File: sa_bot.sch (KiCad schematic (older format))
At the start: 61 parts, among them CON1 MicroSD_Card, P1 USB_OTG, P11 MOTOR_A, P12 MOTOR_B, P13 SONAR_4, P14 SONAR_2, P15 SONAR_3, P17 DBG_CONN, P18 CONN_01X04, P2 BatteryHolder, P3 IR4_JMP, P4 IR2_JMP, P5 IR3_JMP, P6 ExPower, P7 IR_4, P8 IR_2, P9 IR_3, Q1 Q_PMOS_DSG, SW1 SWITCH_INV, SW2 SW_PUSH, SW3 SW_PUSH, SW4 SW_PUSH, U1 74AHC1G125, U2 SAMD21G18, U3 AP2112K-3.3V, U4 NCP1402, U5 DRV8835, Y1 Crystal_Small

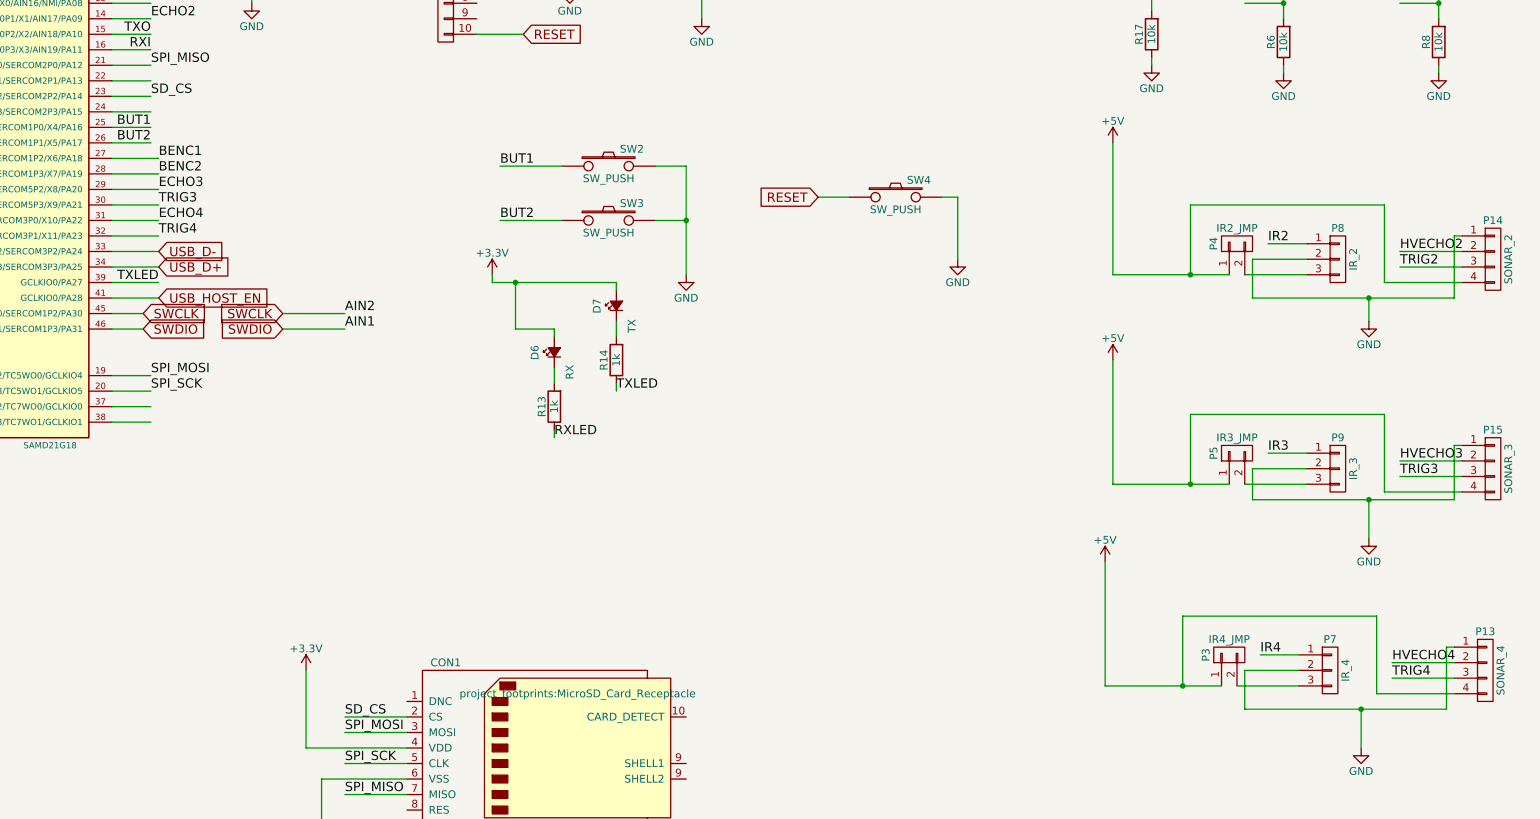
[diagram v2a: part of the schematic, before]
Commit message: Fixed encoder Interrupt
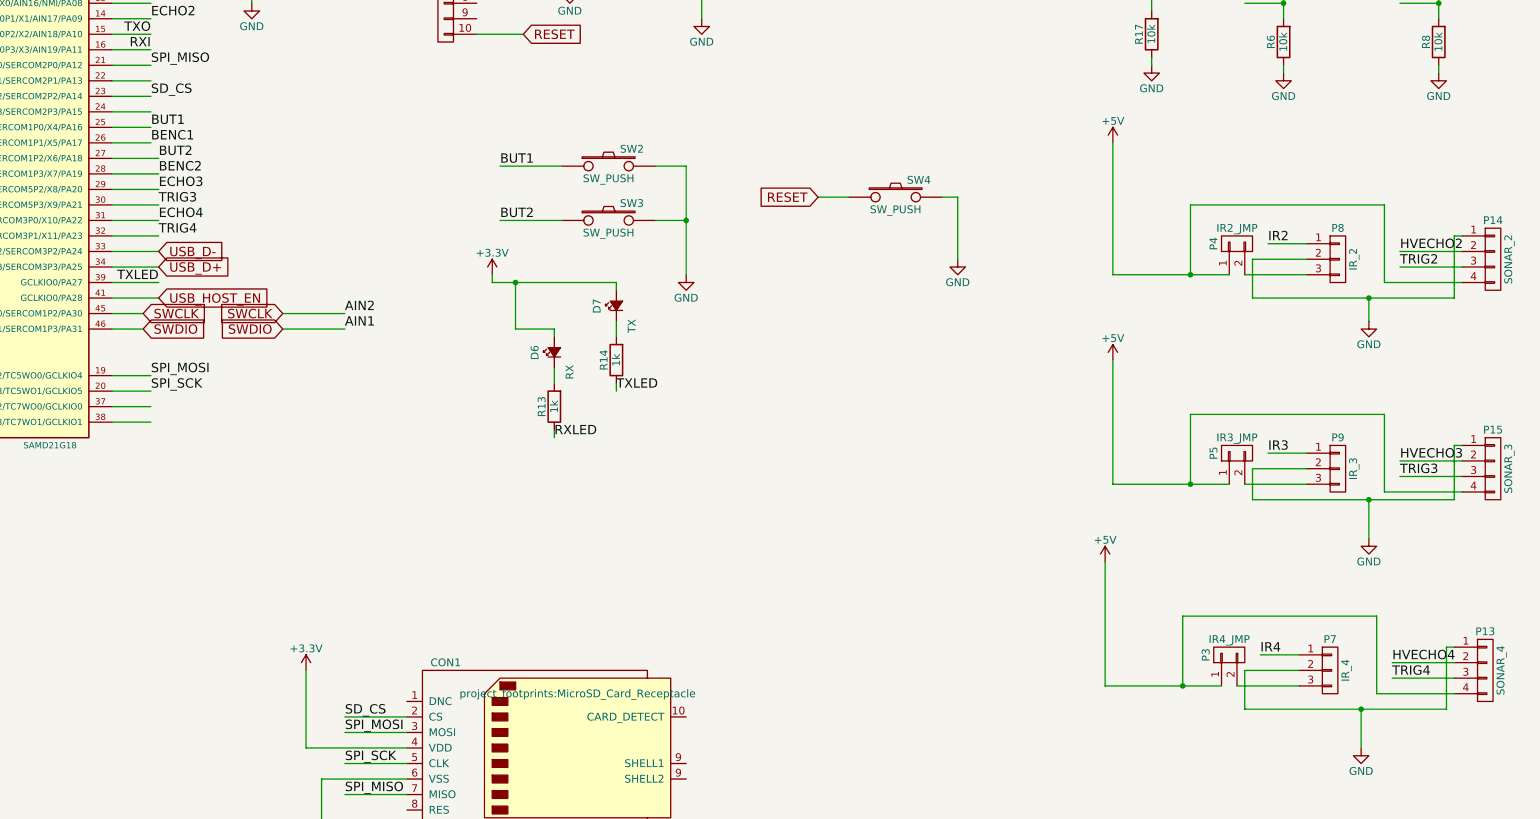
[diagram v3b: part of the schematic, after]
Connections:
- net BENC1: now also U2.26 (GCLKIO3/TC2WO1/SERCOM3P1/SERCOM1P1/X5/PA17); no longer U2.27 (ACCMP0/TC3WO0/SERCOM3P2/SERCOM1P2/X6/PA18)
- net BUT2: now also U2.27 (ACCMP0/TC3WO0/SERCOM3P2/SERCOM1P2/X6/PA18); no longer U2.26 (GCLKIO3/TC2WO1/SERCOM3P1/SERCOM1P1/X5/PA17)

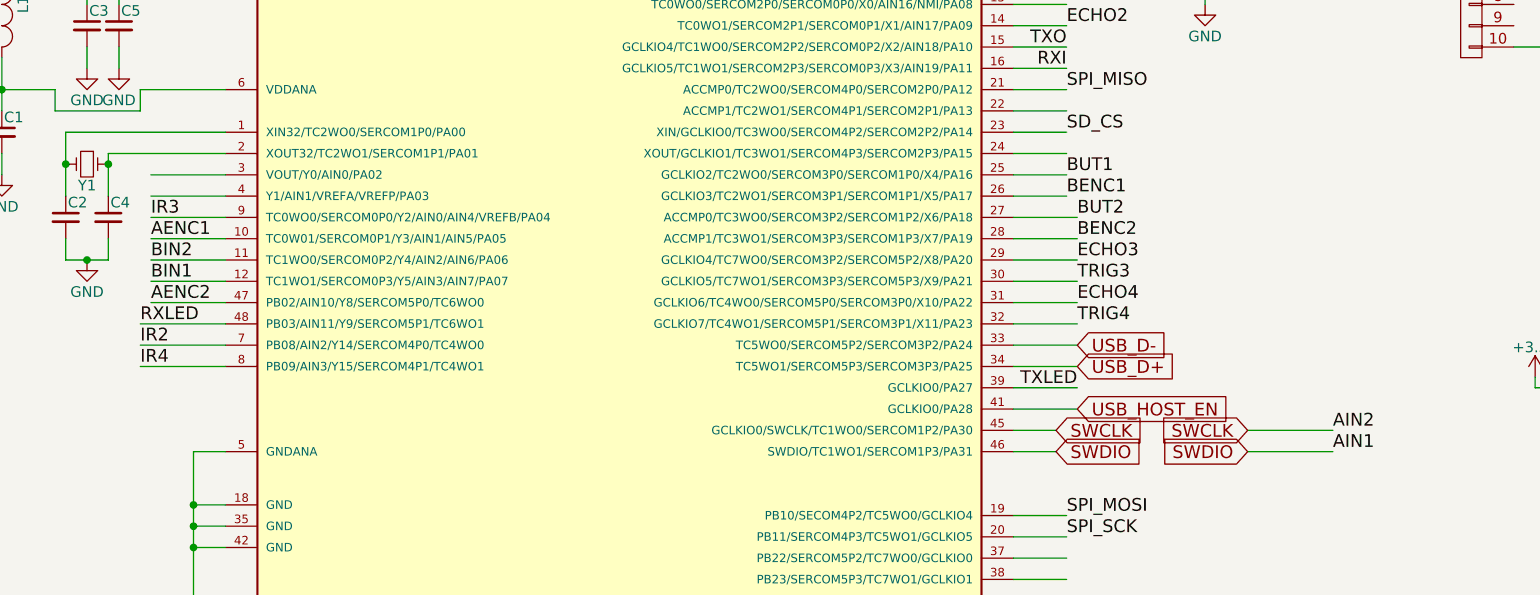
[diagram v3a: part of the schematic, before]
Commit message: Moved Motor from SWCLK to A0
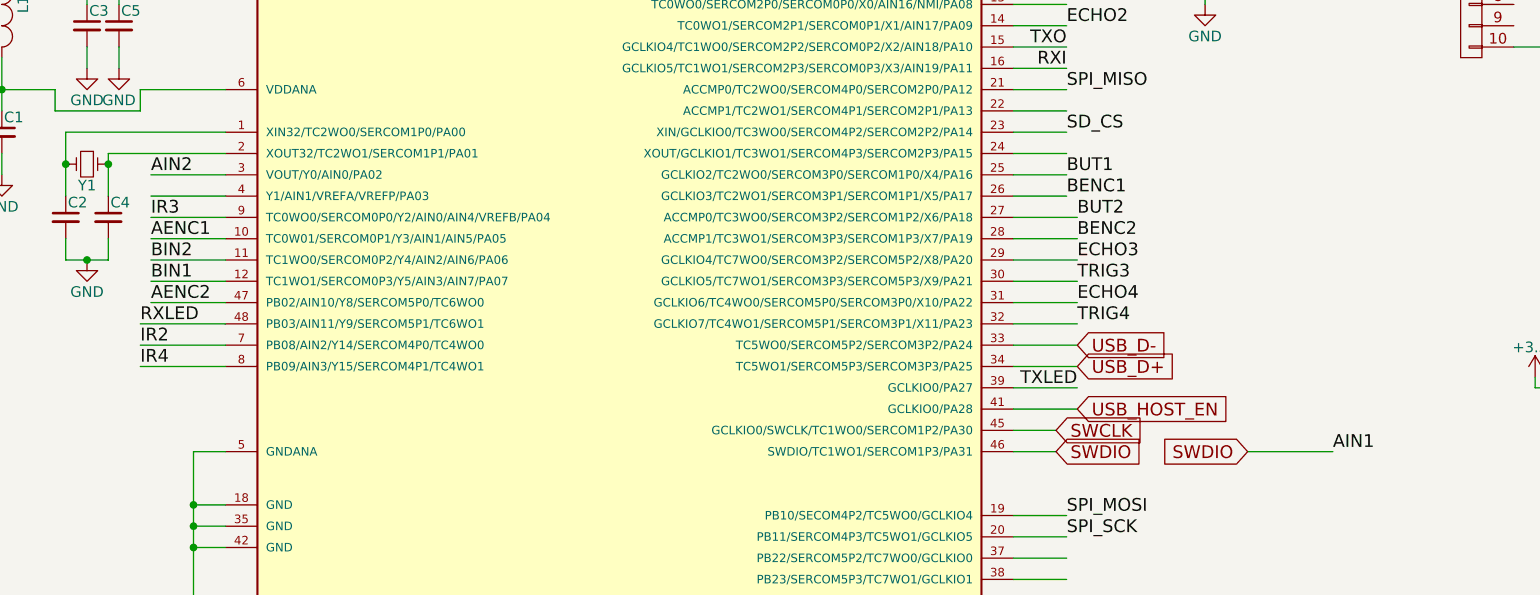
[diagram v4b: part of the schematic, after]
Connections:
- net SWCLK: no longer U5.9 (AIN2)
- net AIN2: now reaches U2.3 (VOUT/Y0/AIN0/PA02)
- net AIN2: now also U5.9 (AIN2)
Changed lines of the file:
@@
 Text Label 1950 3250 0    60   ~ 0
 AENC2
-Text GLabel 7100 3850 0    60   Input ~ 0
-SWCLK
 Text GLabel 7100 3950 0    60   Input ~ 0
 SWDIO
 Text Label 7500 3950 0    60   ~ 0
 AIN1
-Text Label 7500 3850 0    60   ~ 0
+Text Label 1950 2650 0    60   ~ 0
 AIN2
 Text Label 1950 3150 0    60   ~ 0
@@
 	6000 3750 6300 3750
 Wire Wire Line
-	7100 3850 7500 3850
-Wire Wire Line
 	7100 3950 7500 3950
